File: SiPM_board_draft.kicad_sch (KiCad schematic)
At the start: 41 parts, among them J1 Conn_01x01_Pin, J10 Conn_01x01_Pin, J11 Conn_01x01_Pin, J12 Conn_01x01_Pin, J13 Conn_01x01_Pin, J16 Conn_01x01_Pin, J18 Conn_01x01_Pin, J19 Conn_01x01_Pin, J2 Conn_01x01_Pin, J21 Conn_01x01_Pin, J24 Conn_01x01_Pin, J26 Conn_01x01_Pin, J27 Conn_01x01_Pin, J29 Conn_01x01_Pin, J3 Conn_01x01_Pin, J32 Conn_01x01_Pin, J4 Conn_01x01_Pin, J5 Conn_01x01_Pin, J7 Conn_01x01_Pin, J8 Conn_01x01_Pin

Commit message: First draft of full layout with hard-ganged parallel channels, 4 layer, common ground.
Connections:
- net A2 is gone; now on net sigCh5: J24.1 (Pin_1)
- net A8 is gone; now on net sigCh7: J21.1 (Pin_1)
- net B1 is gone; now on net biasCh5: C1.1, R2.1
- net B7 is gone; now on net biasCh7: C2.1, R1.1
- net G1 is gone; now on net sigCh6: J13.1 (Pin_1)
- net G7 is gone; now on net sigCh8: J16.1 (Pin_1)
- net H2 is gone; now on net biasCh6: C7.1, R7.1
- net H8 is gone; now on net biasCh8: C8.1, R8.1
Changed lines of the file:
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@@
+		)
+	)
+	(label "biasCh5"
+		(at 194.31 97.79 0)
+		(effects
+			(font
+				(size 1.27 1.27)
+			)
+			(justify left bottom)
 		)
 	)
@@
 		)
 	)
-	(label "H2"
-		(at 218.44 97.79 180)
-		(effects
-			(font
-				(size 1.27 1.27)
-			)
-			(justify right bottom)
-		)
-	)
 	(label "biasCh7"
 		(at 44.45 87.63 180)
@@
 		)
 	)
+	(label "sigCh5"
+		(at 55.88 175.26 180)
+		(effects
+			(font
+				(size 1.27 1.27)
+			)
+			(justify right bottom)
+		)
+	)
+	(label "sigCh7"
+		(at 55.88 182.88 180)
+		(effects
+			(font
+				(size 1.27 1.27)
+			)
+			(justify right bottom)
+		)
+	)
 	(label "E3"
 		(at 73.66 162.56 0)
@@
 		)
 	)
-	(label "H8"
-		(at 219.71 115.57 180)
-		(effects
-			(font
-				(size 1.27 1.27)
-			)
-			(justify right bottom)
-		)
-	)
 	(label "D3"
 		(at 194.31 64.77 180)
@@
 		)
 	)
-	(label "A8"
-		(at 55.88 182.88 180)
-		(effects
-			(font
-				(size 1.27 1.27)
-			)
-			(justify right bottom)
-		)
-	)
-	(label "G1"
-		(at 73.66 175.26 0)
+	(label "biasCh7"
+		(at 194.31 115.57 0)
 		(effects
 			(font
@@
 		)
 	)
+	(label "biasCh6"
+		(at 218.44 97.79 0)
+		(effects
+			(font
+				(size 1.27 1.27)
+			)
+			(justify left bottom)
+		)
+	)
 	(label "GND"
 		(at 204.47 91.44 0)
@@
 		)
 	)
-	(label "G7"
-		(at 73.66 182.88 0)
-		(effects
-			(font
-				(size 1.27 1.27)
-			)
-			(justify left bottom)
-		)
-	)
 	(label "biasCh6"
 		(at 87.63 77.47 0)
@@
 		)
 	)
-	(label "A2"
-		(at 55.88 175.26 180)
-		(effects
-			(font
-				(size 1.27 1.27)
-			)
-			(justify right bottom)
-		)
-	)
 	(label "biasCh5"
 		(at 44.45 95.25 180)
@@
 		)
 	)
-	(label "B1"
-		(at 194.31 97.79 180)
-		(effects
-			(font
-				(size 1.27 1.27)
-			)
-			(justify right bottom)
-		)
-	)
 	(label "preF_Ch4"
 		(at 92.71 165.1 180)
@@
 		)
 	)
+	(label "biasCh8"
+		(at 219.71 115.57 0)
+		(effects
+			(font
+				(size 1.27 1.27)
+			)
+			(justify left bottom)
+		)
+	)
 	(label "A6"
 		(at 55.88 180.34 180)
@@
 		)
 	)
+	(label "sigCh8"
+		(at 73.66 182.88 0)
+		(effects
+			(font
+				(size 1.27 1.27)
+			)
+			(justify left bottom)
+		)
+	)
 	(label "preF_Ch3"
 		(at 194.31 91.44 0)
@@
 		)
 	)
+	(label "sigCh6"
+		(at 73.66 175.26 0)
+		(effects
+			(font
+				(size 1.27 1.27)
+			)
+			(justify left bottom)
+		)
+	)
 	(label "biasCh8"
 		(at 87.63 87.63 0)
@@
 		(effects
 			(font
-				(size 1.27 1.27)
-			)
-			(justify right bottom)
-		)
-	)
-	(label "B7"
-		(at 194.31 115.57 180)
-		(effects
-			(font

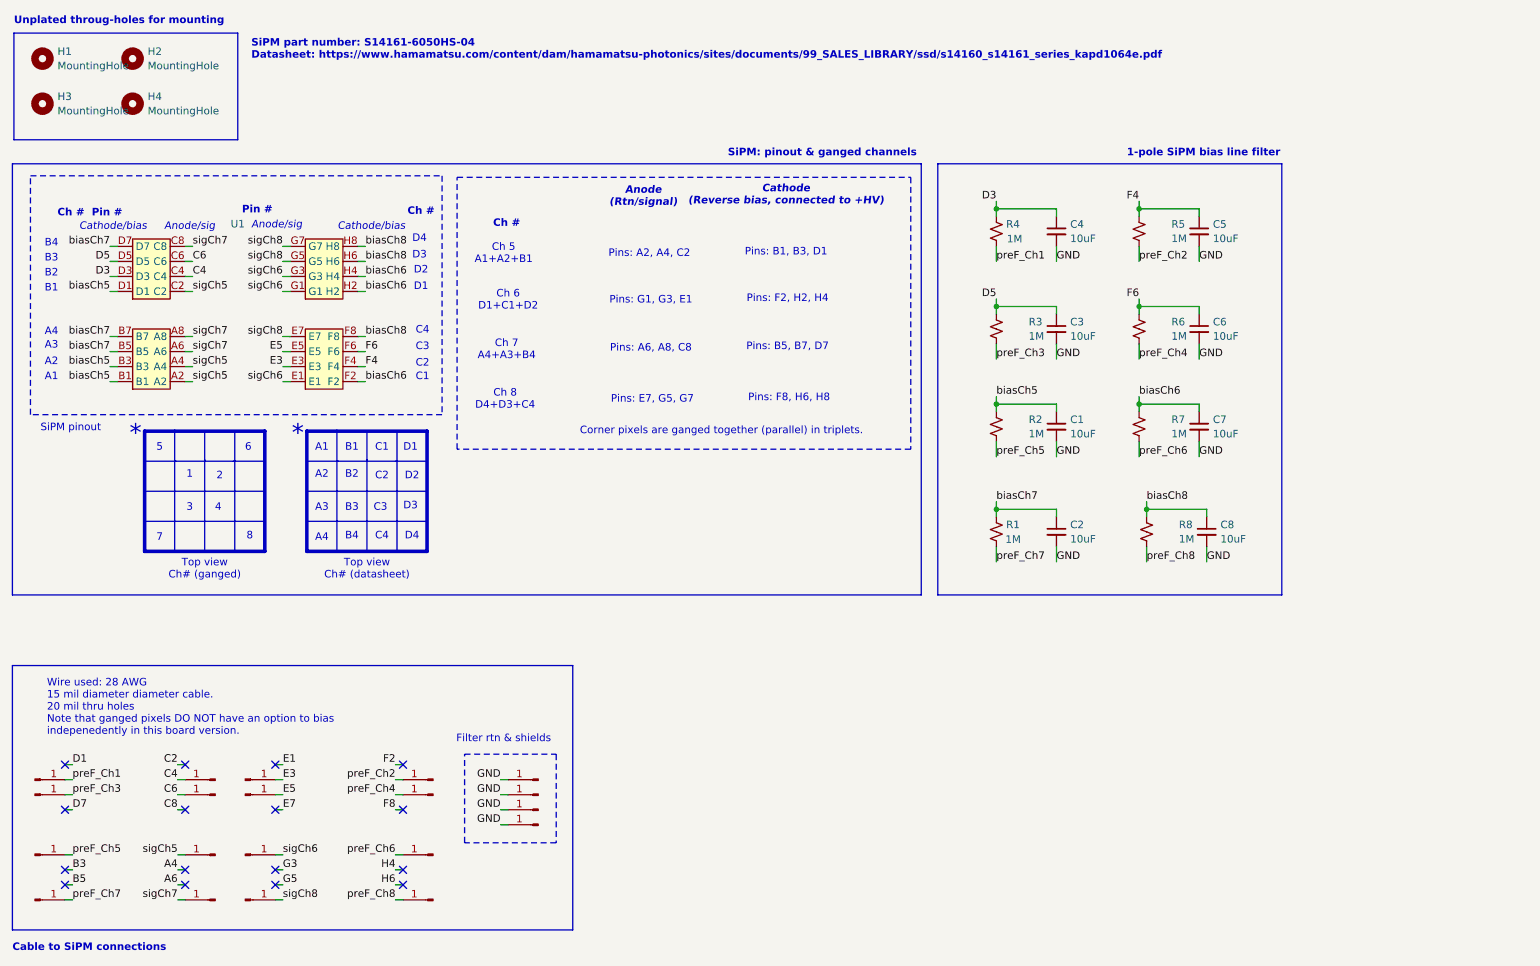
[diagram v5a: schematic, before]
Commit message: First draft of board v2.1. Made caps all 0806, should be good for either 4.7uF at 50V or 2.2uF at 100V. Either way, sufficient for this application. This was done to decrease the vertical footprint of the board and increase the clearance to the SiPM: partially to reduce the risk of the caps shorting to the detector but alsp to provide sufficient clearance for the scintiallator.
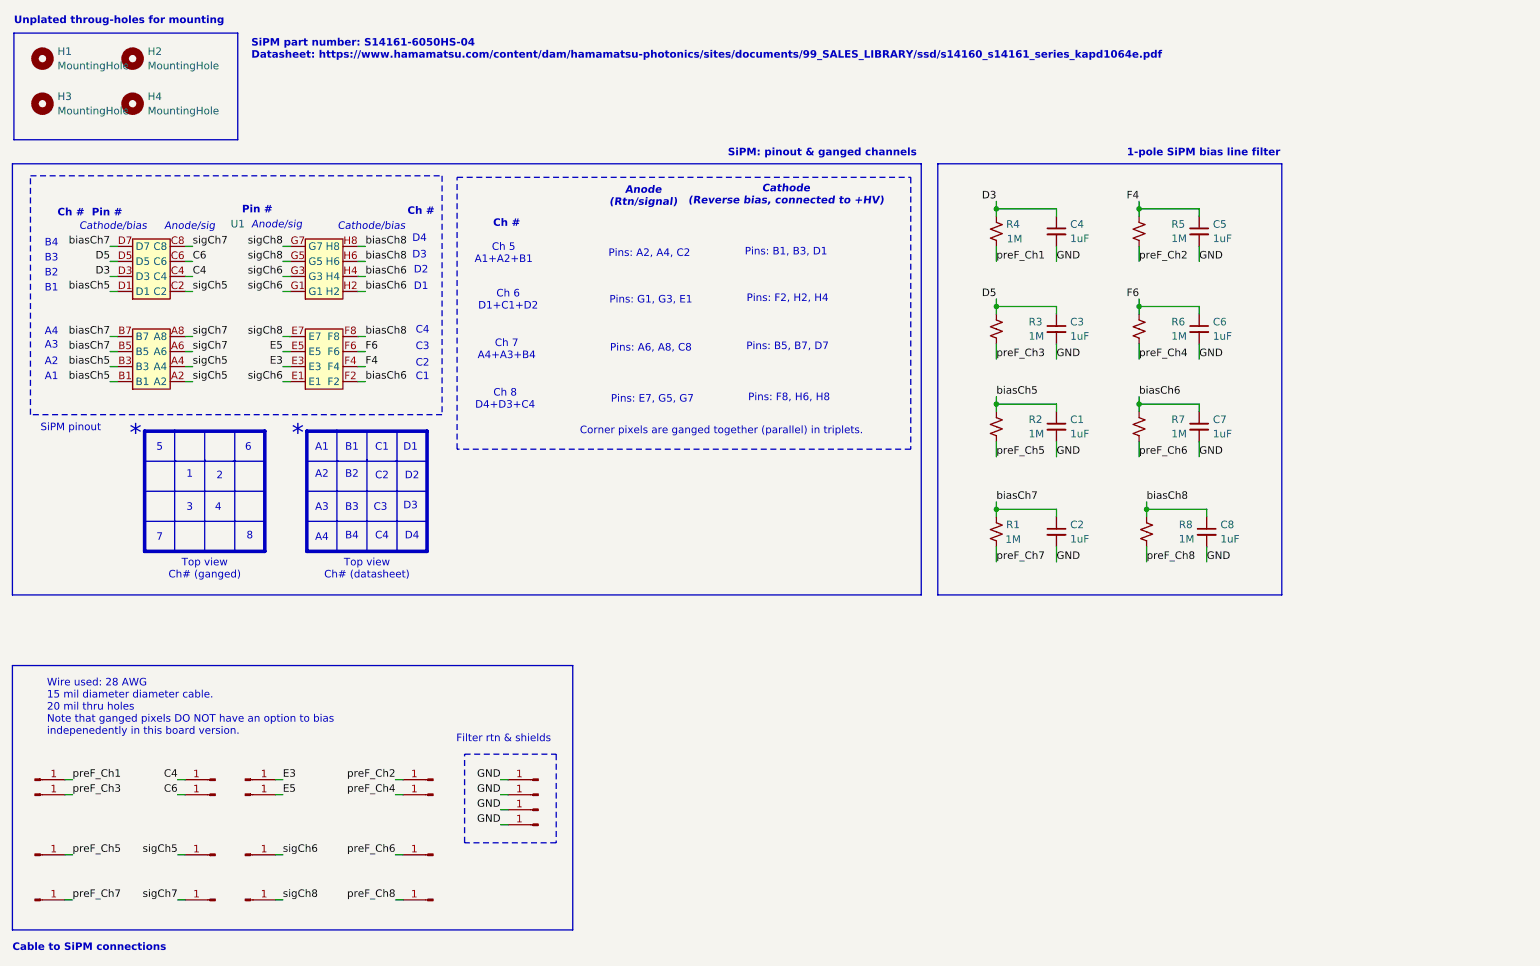
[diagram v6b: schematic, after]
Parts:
- C1, C2, C3, C4, C5, C6, C7, C8: value 10uF -> 1uF; footprint Capacitor_SMD:C_1210_3225Metric -> Capacitor_SMD:C_0805_2012Metric
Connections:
- no-connect marks 16 -> 0
